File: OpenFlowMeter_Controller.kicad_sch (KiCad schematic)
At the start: 35 parts, among them J3 Conn_01x06, J5 Conn_01x03, J6 Conn_02x04_Odd_Even, J7 Conn_02x03_Odd_Even, U2 STM32F103C8Tx, U5 SN65HVD231, U7 24LC64, Y1 12 MHz

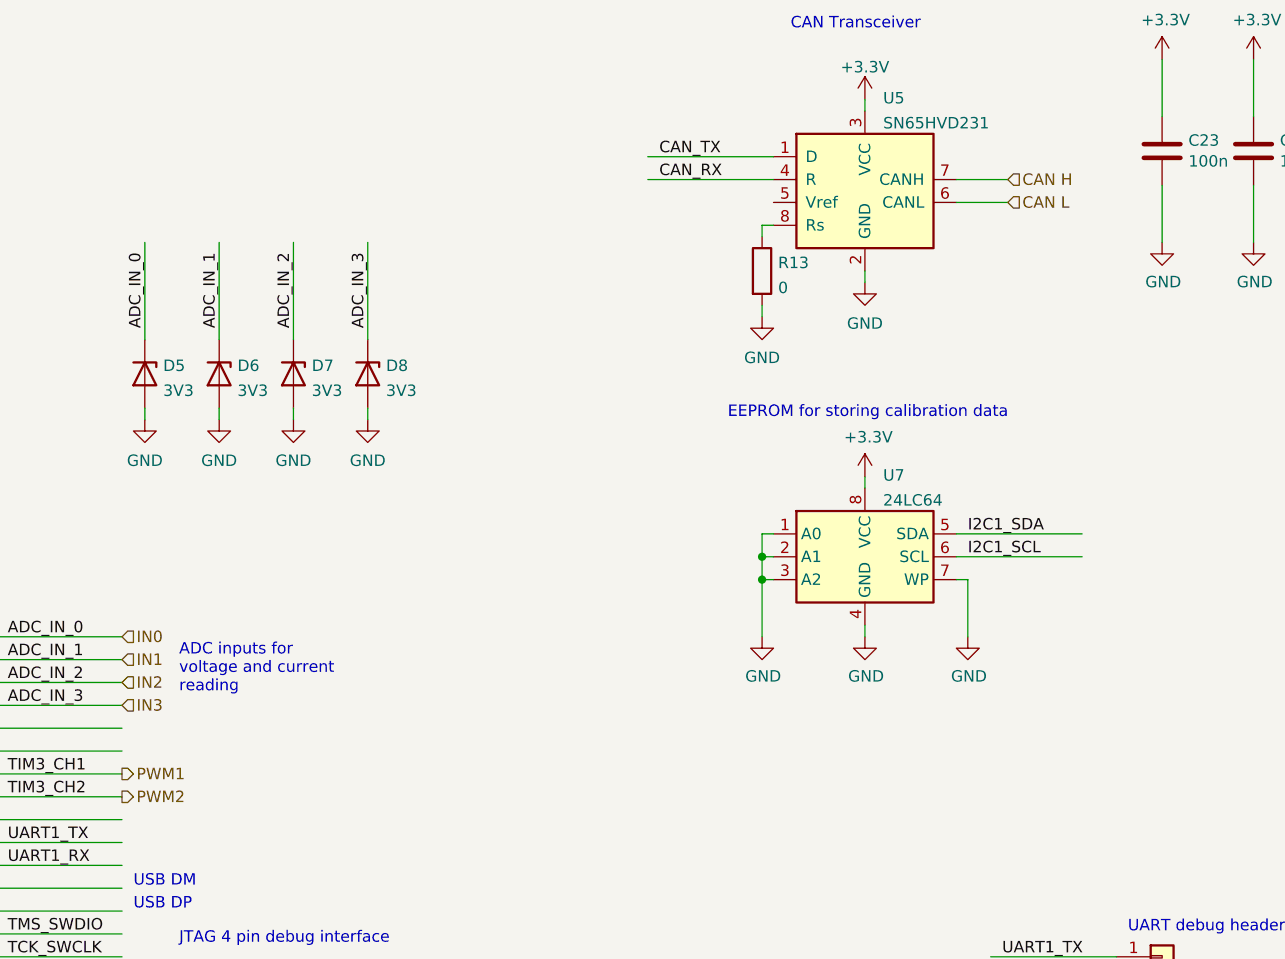
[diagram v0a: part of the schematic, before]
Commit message: added write protection to EEPROM
added jumper, which can be opened and then the EEPROM is write protected.
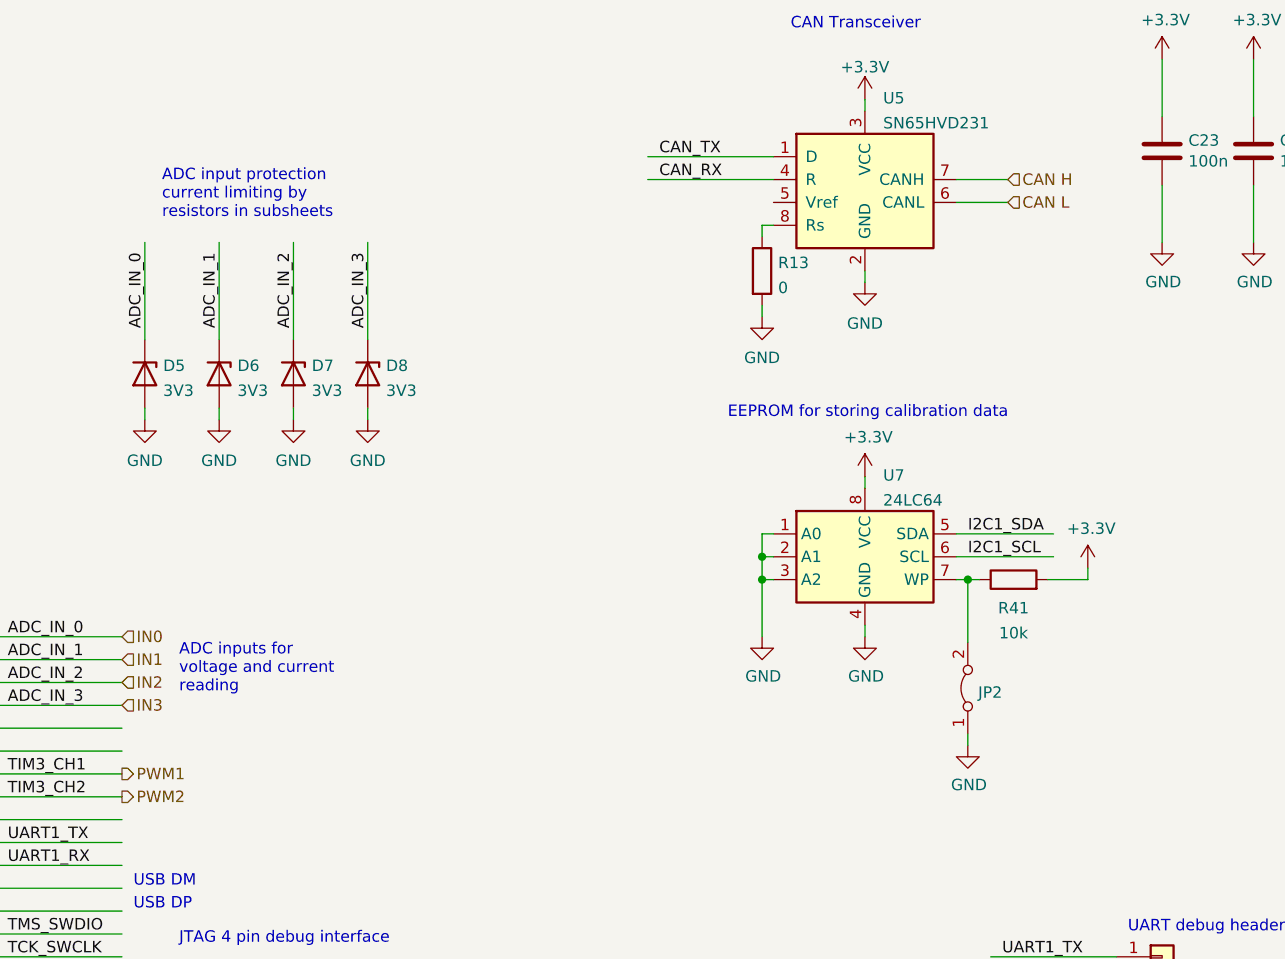
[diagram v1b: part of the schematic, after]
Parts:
- added JP2: Jumper_2_Bridged, Jumper:SolderJumper-2_P1.3mm_Bridged_RoundedPad1.0x1.5mm, symbol Jumper:Jumper_2_Bridged
- added R41: 10k, Resistor_SMD:R_0603_1608Metric, symbol Device:R
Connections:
- net +3V3: now also R41.2
- net GND: now also JP2.1 (A); no longer U7.7 (WP)
- new net: JP2.2 (B), R41.1, U7.7 (WP)
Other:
- note added: "ADC input protection current limiting by resistors in subsheets"
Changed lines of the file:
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@@
   (junction (at 118.11 128.27) (diameter 0) (color 0 0 0 0)
   )
+  (junction (at 243.84 77.47) (diameter 0) (color 0 0 0 0)
+  )
   (junction (at 220.98 74.93) (diameter 0) (color 0 0 0 0)
   )
@@
     (stroke (width 0) (type default) (color 0 0 0 0))
   )
+  (wire (pts (xy 243.84 77.47) (xy 243.84 84.455))
+    (stroke (width 0) (type default) (color 0 0 0 0))
+  )
   (wire (pts (xy 220.98 74.93) (xy 220.98 72.39))
     (stroke (width 0) (type default) (color 0 0 0 0))
@@
     (stroke (width 0) (type default) (color 0 0 0 0))
   )
+  (wire (pts (xy 252.73 77.47) (xy 257.175 77.47))
+    (stroke (width 0) (type default) (color 0 0 0 0))
+  )
   (wire (pts (xy 88.9 109.22) (xy 102.87 109.22))
     (stroke (width 0) (type default) (color 0 0 0 0))
@@
     (stroke (width 0) (type default) (color 0 0 0 0))
   )
-  (wire (pts (xy 242.57 72.39) (xy 256.54 72.39))
+  (wire (pts (xy 242.57 72.39) (xy 253.365 72.39))
     (stroke (width 0) (type default) (color 0 0 0 0))
   )
@@
     (stroke (width 0) (type default) (color 0 0 0 0))
   )
-  (wire (pts (xy 243.84 77.47) (xy 243.84 83.82))
-    (stroke (width 0) (type default) (color 0 0 0 0))
-  )
   (wire (pts (xy 135.89 83.82) (xy 149.86 83.82))
     (stroke (width 0) (type default) (color 0 0 0 0))
@@
     (stroke (width 0) (type default) (color 0 0 0 0))
   )
+  (wire (pts (xy 257.175 77.47) (xy 257.175 76.2))
+    (stroke (width 0) (type default) (color 0 0 0 0))
+  )
   (wire (pts (xy 118.11 49.53) (xy 115.57 49.53))
     (stroke (width 0) (type default) (color 0 0 0 0))
@@
     (stroke (width 0) (type default) (color 0 0 0 0))
   )
+  (wire (pts (xy 243.84 94.615) (xy 243.84 95.885))
+    (stroke (width 0) (type default) (color 0 0 0 0))
+  )
   (wire (pts (xy 135.89 109.22) (xy 149.86 109.22))
     (stroke (width 0) (type default) (color 0 0 0 0))
@@
     (stroke (width 0) (type default) (color 0 0 0 0))
   )
-  (wire (pts (xy 242.57 74.93) (xy 256.54 74.93))
+  (wire (pts (xy 242.57 74.93) (xy 253.365 74.93))
     (stroke (width 0) (type default) (color 0 0 0 0))
   )
@@
     (stroke (width 0) (type default) (color 0 0 0 0))
   )
+  (wire (pts (xy 243.84 77.47) (xy 245.11 77.47))
+    (stroke (width 0) (type default) (color 0 0 0 0))
+  )
   (wire (pts (xy 38.1 74.93) (xy 38.1 76.2))
     (stroke (width 0) (type default) (color 0 0 0 0))
@@
   )
   (text "SPI for extension" (at 27.94 149.86 0)
+    (effects (font (size 1.27 1.27)) (justify left bottom))
+  )
+  (text "ADC input protection\ncurrent limiting by \nresistors in subsheets"
+    (at 154.305 37.465 0)
     (effects (font (size 1.27 1.27)) (justify left bottom))
   )
@@
     )
     (pin "1")
+  )
+  (symbol (lib_id "Jumper:Jumper_2_Bridged") (at 243.84 89.535 90) (unit 1)
+    (in_bom yes) (on_board yes) (fields_autoplaced)
+    (property "Reference" "JP2" (id 0) (at 244.983 90.014 90)
+      (effects (font (size 1.27 1.27)) (justify right))
+    )
+    (property "Value" "Jumper_2_Bridged" (id 1) (at 244.983 91.4016 90)
+      (effects (font (size 1.27 1.27)) (justify right) hide)
+    )
+    (property "Footprint" "Jumper:SolderJumper-2_P1.3mm_Bridged_RoundedPad1.0x1.5mm" (id 2) (at 243.84 89.535 0)
+      (effects (font (size 1.27 1.27)) hide)
+    )
+    (property "Datasheet" "~" (id 3) (at 243.84 89.535 0)
+      (effects (font (size 1.27 1.27)) hide)
+    )
+    (pin "1")
+    (pin "2")
   )
   (symbol (lib_id "Device:R") (at 109.22 158.75 0) (unit 1)
@@
     (pin "1")
   )
+  (symbol (lib_id "power:GND") (at 243.84 95.885 0) (unit 1)
+    (in_bom yes) (on_board yes)
+    (property "Reference" "#PWR0122" (id 0) (at 243.84 102.235 0)
+      (effects (font (size 1.27 1.27)) hide)
+    )
+    (property "Value" "GND" (id 1) (at 243.967 100.2792 0))
+    (property "Footprint" "" (id 2) (at 243.84 95.885 0)
+      (effects (font (size 1.27 1.27)) hide)
+    )
+    (property "Datasheet" "" (id 3) (at 243.84 95.885 0)
+      (effects (font (size 1.27 1.27)) hide)
+    )
+    (pin "1")
+  )
   (symbol (lib_id "power:GND") (at 160.655 59.69 0) (unit 1)
     (in_bom yes) (on_board yes) (fields_autoplaced)
@@
     (pin "1")
   )
-  (symbol (lib_id "power:GND") (at 243.84 83.82 0) (unit 1)
-    (in_bom yes) (on_board yes)
-    (property "Reference" "#PWR061" (id 0) (at 243.84 90.17 0)
-      (effects (font (size 1.27 1.27)) hide)
-    )
-    (property "Value" "GND" (id 1) (at 243.967 88.2142 0))
-    (property "Footprint" "" (id 2) (at 243.84 83.82 0)
-      (effects (font (size 1.27 1.27)) hide)
-    )
-    (property "Datasheet" "" (id 3) (at 243.84 83.82 0)
-      (effects (font (size 1.27 1.27)) hide)
-    )
-    (pin "1")
-  )
   (symbol (lib_id "Device:C") (at 82.55 55.88 90) (unit 1)
     (in_bom yes) (on_board yes)
@@
     (pin "2")
   )
+  (symbol (lib_id "Device:R") (at 248.92 77.47 90) (unit 1)
+    (in_bom yes) (on_board yes) (fields_autoplaced)
+    (property "Reference" "R41" (id 0) (at 248.92 80.6355 90))
+    (property "Value" "10k" (id 1) (at 248.92 83.4106 90))
+    (property "Footprint" "Resistor_SMD:R_0603_1608Metric" (id 2) (at 248.92 79.248 90)
+      (effects (font (size 1.27 1.27)) hide)
+    )
+    (property "Datasheet" "~" (id 3) (at 248.92 77.47 0)
+      (effects (font (size 1.27 1.27)) hide)
+    )
+    (pin "1")
+    (pin "2")
+  )
   (symbol (lib_id "power:+3.3V") (at 275.59 19.685 0) (unit 1)
     (in_bom yes) (on_board yes)
@@
     (pin "2")
   )
+  (symbol (lib_id "power:+3.3V") (at 257.175 76.2 0) (unit 1)
+    (in_bom yes) (on_board yes)
+    (property "Reference" "#PWR0123" (id 0) (at 257.175 80.01 0)
+      (effects (font (size 1.27 1.27)) hide)
+    )
+    (property "Value" "+3.3V" (id 1) (at 257.556 71.8058 0))
+    (property "Footprint" "" (id 2) (at 257.175 76.2 0)
+      (effects (font (size 1.27 1.27)) hide)
+    )
+    (property "Datasheet" "" (id 3) (at 257.175 76.2 0)
+      (effects (font (size 1.27 1.27)) hide)
+    )
+    (pin "1")
+  )
   (symbol (lib_id "power:+3.3V") (at 87.63 44.45 0) (unit 1)

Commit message: Some minor cleanups
Removed DRCs and did some minor cleanups.
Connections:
- no-connect marks 0 -> 9
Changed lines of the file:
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@@
   (junction (at 120.65 49.53) (diameter 0) (color 0 0 0 0)
   )
+  (no_connect (at 149.86 104.14))
+  (no_connect (at 149.86 111.76))
+  (no_connect (at 149.86 93.98))
+  (no_connect (at 149.86 96.52))
+  (no_connect (at 149.86 114.3))
+  (no_connect (at 88.9 73.66))
+  (no_connect (at 88.9 76.2))
+  (no_connect (at 88.9 78.74))
+  (no_connect (at 220.98 35.56))
   (wire (pts (xy 96.52 162.56) (xy 96.52 165.1))
     (stroke (width 0) (type default) (color 0 0 0 0))
@@
   )
   (wire (pts (xy 118.11 127) (xy 118.11 128.27))
+    (stroke (width 0) (type default) (color 0 0 0 0))
+  )
+  (wire (pts (xy 220.98 35.56) (xy 222.25 35.56))
     (stroke (width 0) (type default) (color 0 0 0 0))
   )
@@
     (pin "1")
   )
-  (symbol (lib_id "Graphic:Logo_Open_Hardware_Small") (at 166.37 189.23 0) (unit 1)
-    (in_bom yes) (on_board yes) (fields_autoplaced)
-    (property "Reference" "#LOGO1" (id 0) (at 166.37 182.245 0)
-      (effects (font (size 1.27 1.27)) hide)
-    )
-    (property "Value" "Logo_Open_Hardware_Small" (id 1) (at 166.37 194.945 0)
-      (effects (font (size 1.27 1.27)) hide)
-    )
-    (property "Footprint" "" (id 2) (at 166.37 189.23 0)
-      (effects (font (size 1.27 1.27)) hide)
-    )
-    (property "Datasheet" "~" (id 3) (at 166.37 189.23 0)
-      (effects (font (size 1.27 1.27)) hide)
-    )
-  )
   (symbol (lib_id "power:+3.3V") (at 59.69 25.4 0) (unit 1)

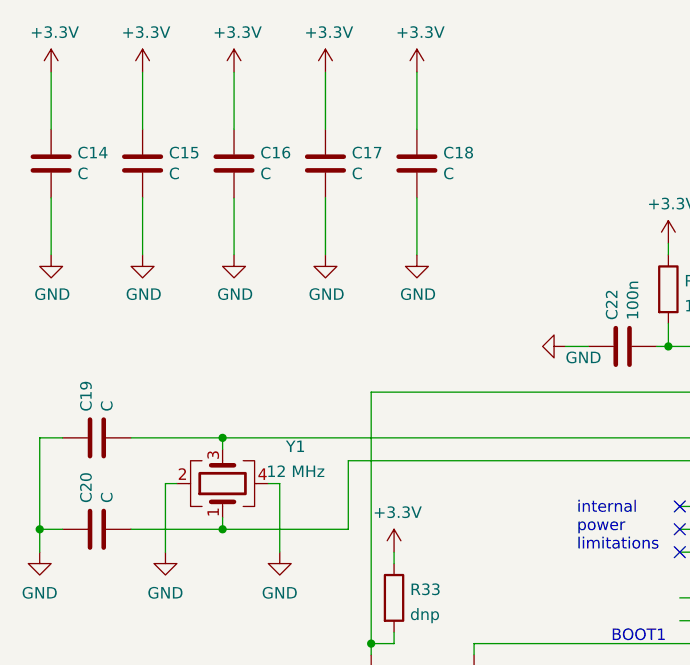
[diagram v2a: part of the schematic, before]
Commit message: included values from simulation
added values to those components, which did not had one
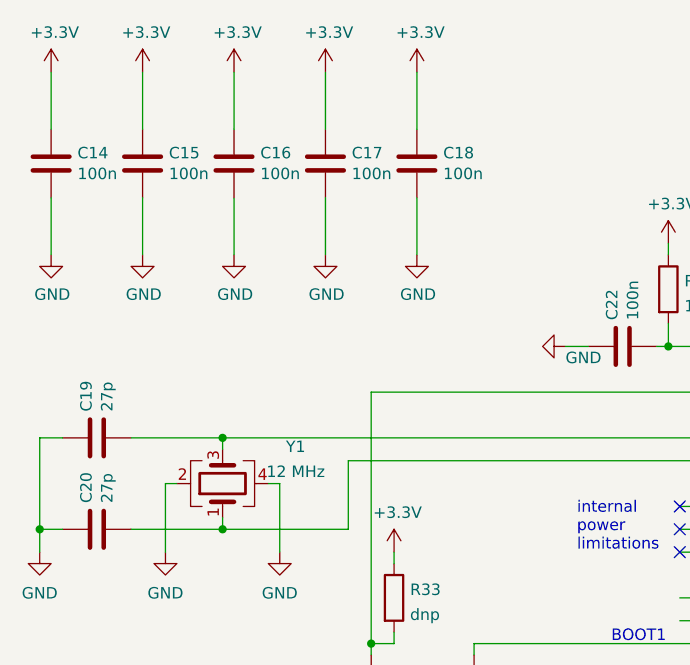
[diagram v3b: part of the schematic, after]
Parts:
- C14, C15, C16, C17, C18: value C -> 100n
- C19, C20: value C -> 27p
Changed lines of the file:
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@@
       (effects (font (size 1.27 1.27)) (justify left))
     )
-    (property "Value" "C" (id 1) (at 42.291 36.703 0)
+    (property "Value" "100n" (id 1) (at 42.291 36.703 0)
       (effects (font (size 1.27 1.27)) (justify left))
     )
@@
       (effects (font (size 1.27 1.27)) (justify left))
     )
-    (property "Value" "C" (id 1) (at 32.131 36.703 0)
+    (property "Value" "100n" (id 1) (at 32.131 36.703 0)
       (effects (font (size 1.27 1.27)) (justify left))
     )
@@
       (effects (font (size 1.27 1.27)) (justify left))
     )
-    (property "Value" "C" (id 1) (at 25.273 63.119 0)
+    (property "Value" "27p" (id 1) (at 25.273 63.119 0)
       (effects (font (size 1.27 1.27)) (justify left))
     )
@@
       (effects (font (size 1.27 1.27)) (justify left))
     )
-    (property "Value" "C" (id 1) (at 62.611 36.703 0)
+    (property "Value" "100n" (id 1) (at 62.611 36.703 0)
       (effects (font (size 1.27 1.27)) (justify left))
     )
@@
       (effects (font (size 1.27 1.27)) (justify left))
     )
-    (property "Value" "C" (id 1) (at 52.451 36.703 0)
+    (property "Value" "100n" (id 1) (at 52.451 36.703 0)
       (effects (font (size 1.27 1.27)) (justify left))
     )
@@
       (effects (font (size 1.27 1.27)) (justify left))
     )
-    (property "Value" "C" (id 1) (at 25.273 73.279 0)
+    (property "Value" "27p" (id 1) (at 25.273 73.279 0)
       (effects (font (size 1.27 1.27)) (justify left))
     )
@@
       (effects (font (size 1.27 1.27)) (justify left))
     )
-    (property "Value" "C" (id 1) (at 21.971 36.703 0)
-      (effects (font (size 1.27 1.27)) (justify left))
-    )
+    (property "Value" "100n" (id 1) (at 21.971 36.703 0)
+      (effects (font (size 1.27 1.27)) (justify left))
+    )
